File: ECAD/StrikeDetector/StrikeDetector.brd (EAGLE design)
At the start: 100 x 80 mm, 32 parts, among them J1 10118193-0001LF, U1 MMBT2222A-7-F, U2 MMBT2222A-7-F, U3 LSM9DS1TR, U4 ESP32-WROOM-32, U6 AP2112K-3.3TRG1

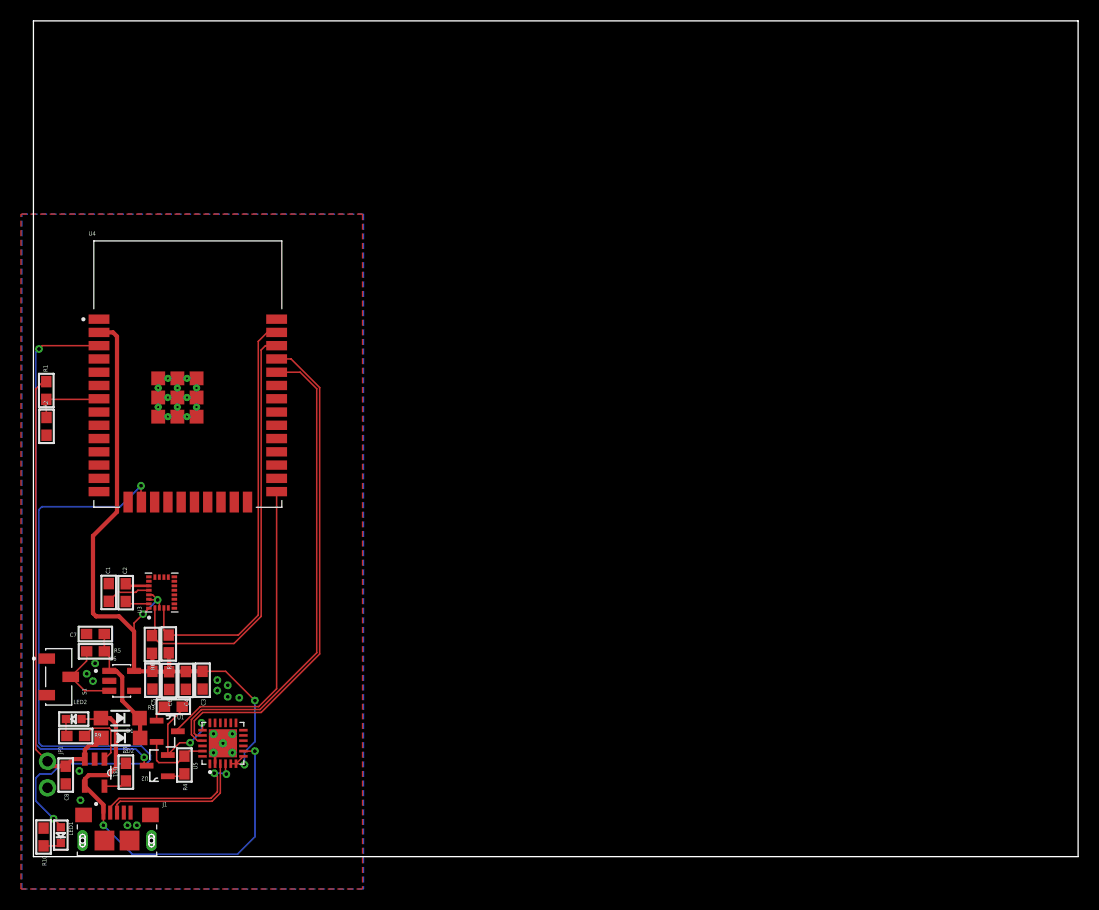
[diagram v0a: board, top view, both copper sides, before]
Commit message: Added dimension
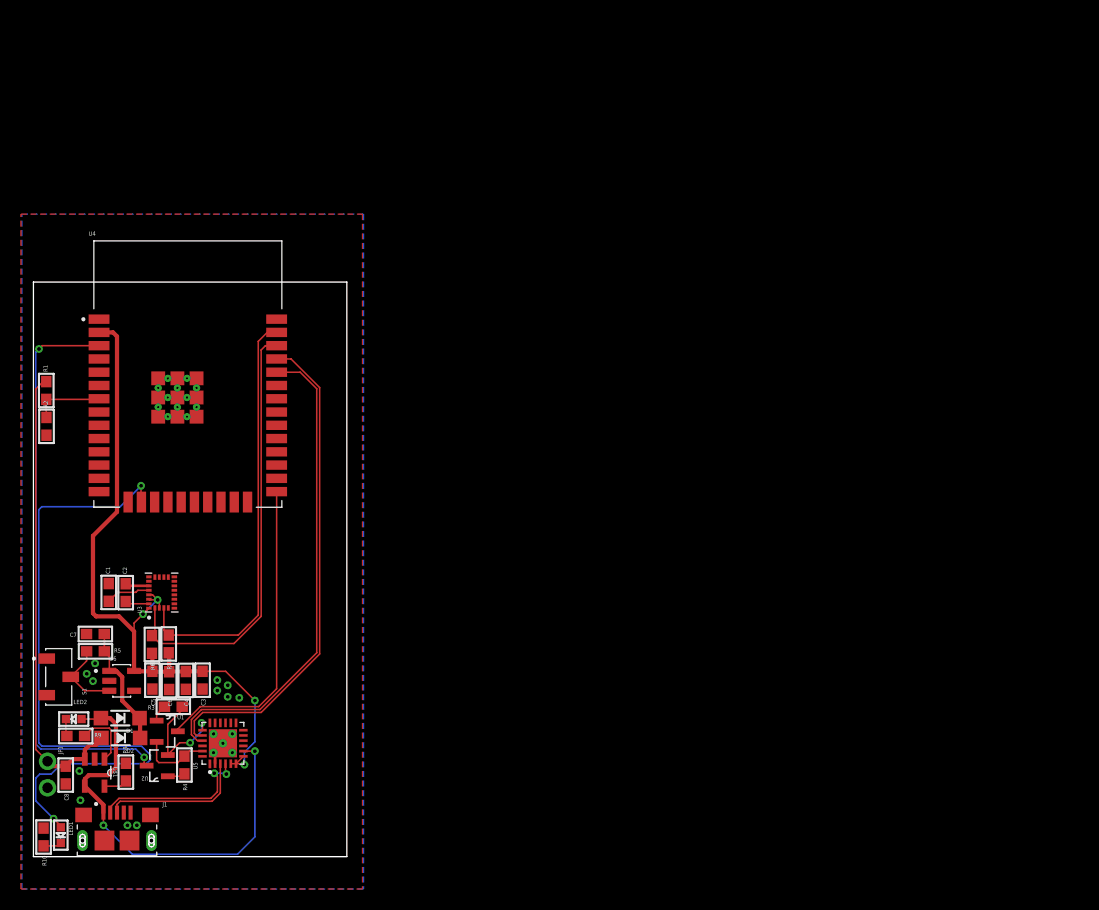
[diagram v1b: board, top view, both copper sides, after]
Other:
- board size 100 x 80 mm -> 30 x 55 mm
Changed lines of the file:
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@@
 <drawing>
 <settings>
-<setting alwaysvectorfont="no"/>
+<setting alwaysvectorfont="yes"/>
 <setting verticaltext="up"/>
 </settings>
@@
 <board>
 <plain>
-<wire x1="0" y1="0" x2="100" y2="0" width="0" layer="20"/>
-<wire x1="100" y1="0" x2="100" y2="80" width="0" layer="20"/>
-<wire x1="100" y1="80" x2="0" y2="80" width="0" layer="20"/>
-<wire x1="0" y1="80" x2="0" y2="0" width="0" layer="20"/>
+<wire x1="0" y1="0" x2="30" y2="0" width="0" layer="20"/>
+<wire x1="30" y1="0" x2="30" y2="55" width="0" layer="20"/>
+<wire x1="30" y1="55" x2="0" y2="55" width="0" layer="20"/>
+<wire x1="0" y1="55" x2="0" y2="0" width="0" layer="20"/>
 </plain>
 <attributes>

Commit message: Updated PCB Design
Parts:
- added JP3: (no value), microbuilder:1X06_ROUND
- added R11: 100kΩ, microbuilder:0603
- added SW1, SW2: KMR211GLFS, adafruit:KMR2
- moved C1 6.42 mm to (11.5, 20.5), turned to 270 degrees
- moved C2 6.36 mm to (13.1, 20.5), turned to 270 degrees
- moved U4 5.68 mm to (12.1, 41.2)
- moved R1 5.00 mm to (1.23, 39.6)
- moved R2 5.00 mm to (1.25, 36.2)
- moved J1 4.00 mm to (12.0, 1.54)
- moved R6 3.89 mm to (14.8, 22.0)
- moved R7 3.85 mm to (16.4, 22.0)
- moved U3 1.31 mm to (12.0, 24.0), turned to 180 degrees
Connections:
- new net N$13: JP3.2
- new net N$17: JP3.6
- net 3.3V: now also R11.2
- net GND: now also JP3.1, SW1.1, SW1.3, SW2.1, SW2.3
- net GPIO0: now also SW2.2, SW2.4
- net RESET: now also R11.1, SW1.2, SW1.4
- net RXD0: now also JP3.4
- net TXD0: now also JP3.5
- net VIN: now also JP3.3
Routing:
- net RESET: track 55.6 -> 69.3 mm
- net RXD0: track 47.2 -> 60.7 mm, vias 0 -> 2
- net SCL: track 41.8 -> 28.3 mm
- net SDA: track 40.5 -> 29.2 mm
- net GPIO13: track 63.7 -> 56.0 mm
- net VIN: track 42.0 -> 48.9 mm
- net TXD0: track 47.5 -> 42.1 mm
- net VBAT: track 44.5 -> 39.5 mm
- net GND: track 3.62 -> 8.49 mm
- net N$2: track 13.9 -> 9.87 mm
- net N$3: track 15.5 -> 11.5 mm
- net 3.3V: track 74.3 -> 70.6 mm
- net N$1: track 4.28 -> 1.54 mm
- net BAT_VAL: track 6.86 -> 4.16 mm
- net GPIO0: track 30.1 -> 32.2 mm
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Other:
- board size 30 x 55 mm -> 24 x 48 mm
- board text added: "GND"
- board text added: "OFF"
- board text added: "ON"
- board text added: "RX"
- board text added: "TX"
- board text added: "VBAT"
- board text added: "VIN"
- board text added: "X"
- board text added: "Y"
- board text added: "Z"
